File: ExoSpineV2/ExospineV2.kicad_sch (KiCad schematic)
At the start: 44 parts, among them J1 GPIO, J15 JST PH 2pin, J16 JST PH 2pin, J19 JST PH 3pin, J20 JST PH 3pin, J22 JST PH 2pin, J23 JST PH 2pin, J24 JST PH 2pin, J25 JST PH 3pin, J26 JST PH 3pin, J27 JST PH 4pin, J29 JST PH 3pin, J30 JST PH 2pin, J34 JST PH 3pin, Q10 Q_NMOS_DGS, Q11 Q_NMOS_DGS, Q6 Q_NMOS_DGS, Q7 Q_NMOS_DGS, Q9 Q_NMOS_DGS, U4 74HC00, U5 74HC00, U6 MCP3008, U7 LTC2944, U8 LTC2944

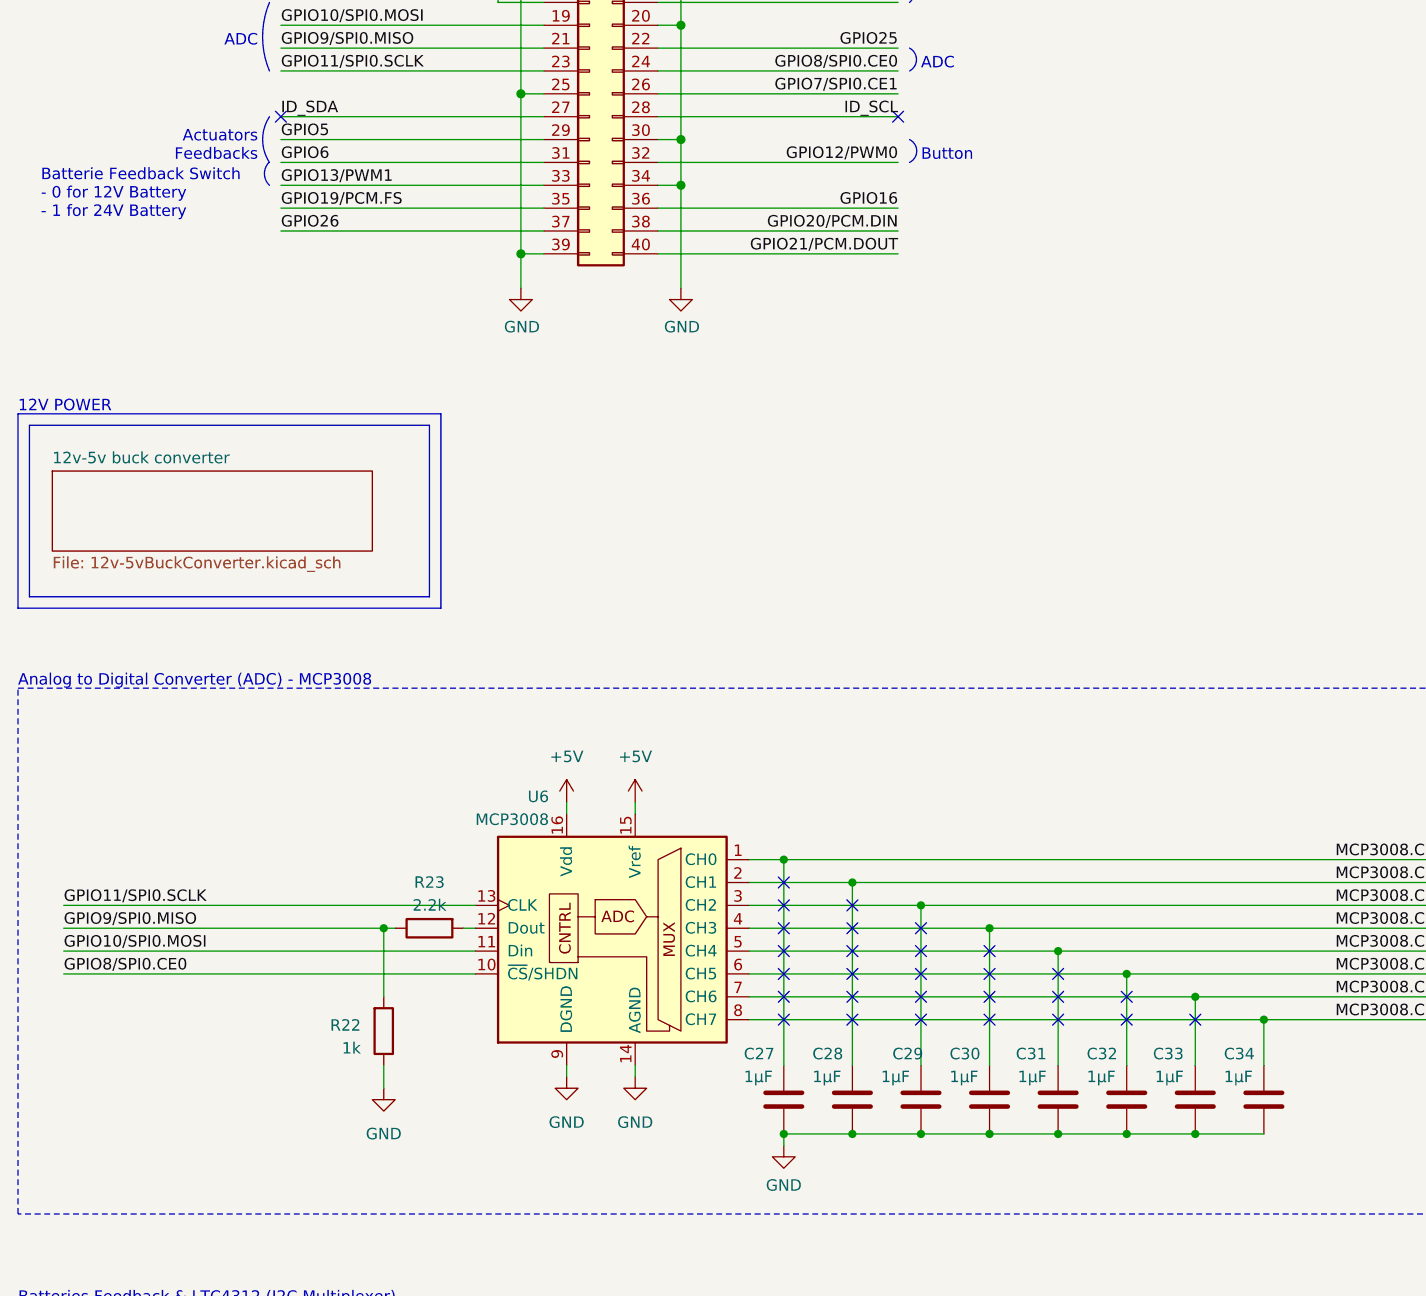
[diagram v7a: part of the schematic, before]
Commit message: chose resistors and capacitors
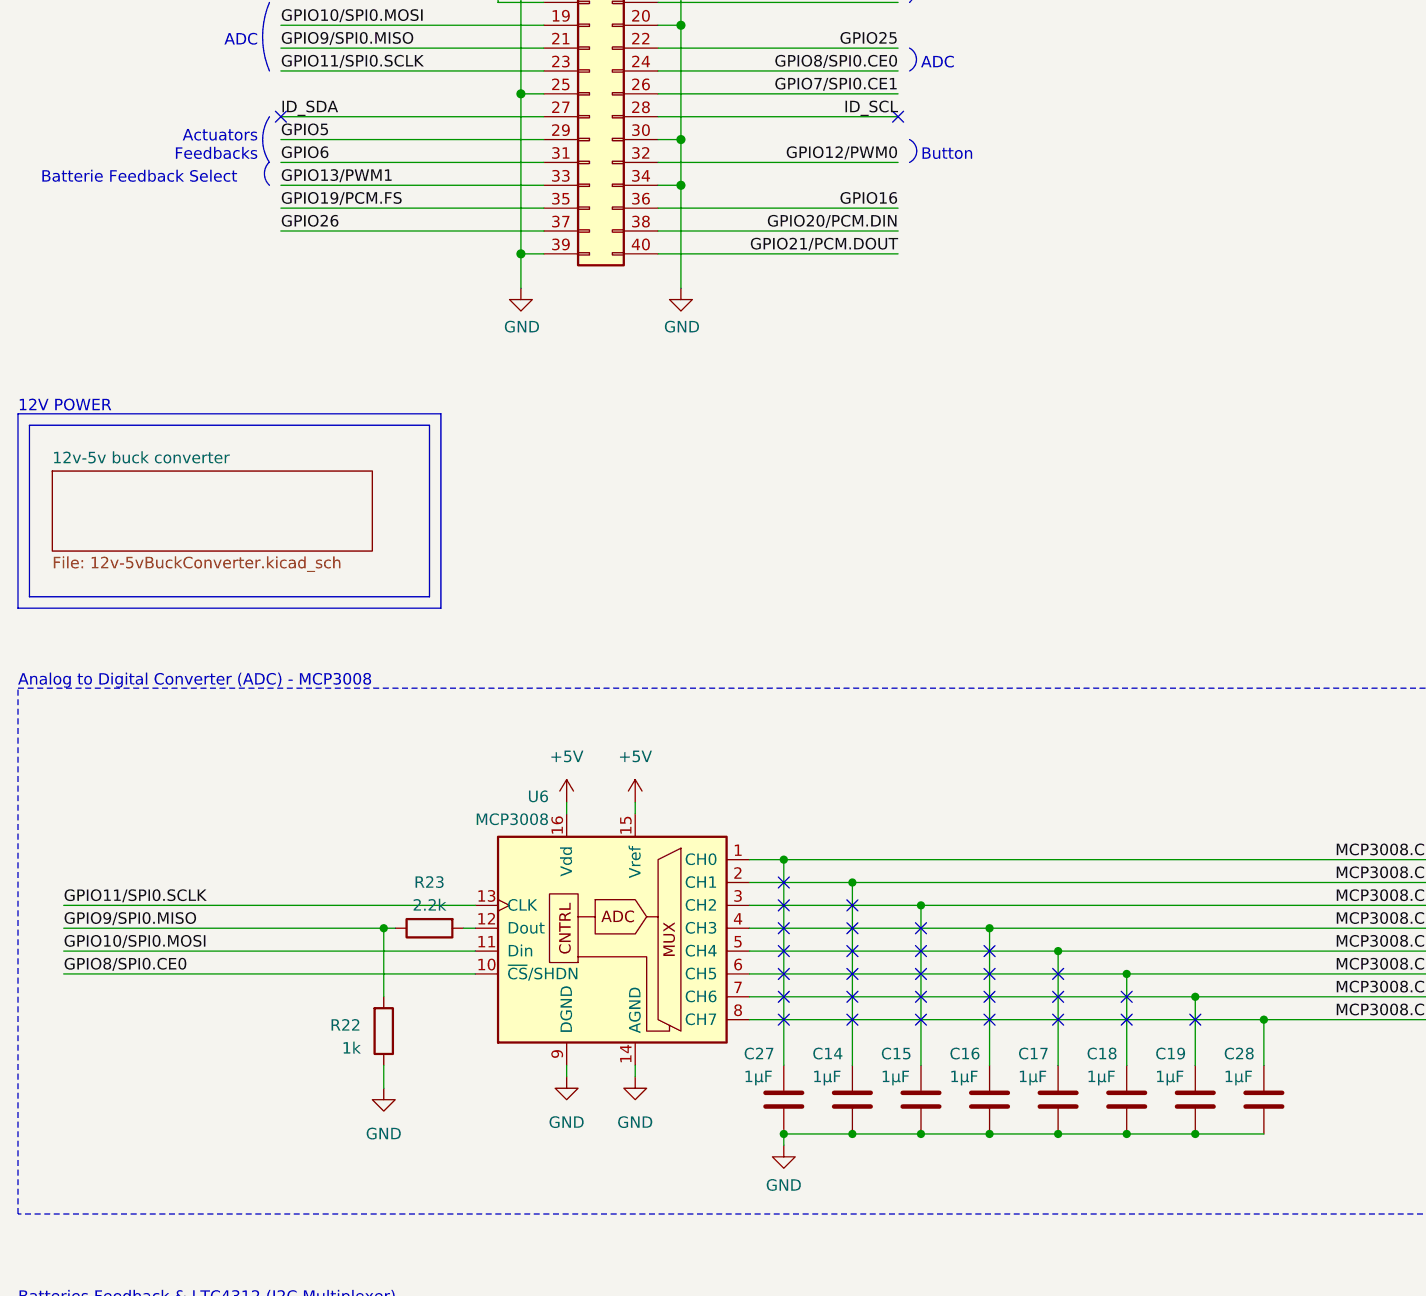
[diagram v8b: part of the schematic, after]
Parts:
- removed C29, C30, C31, C32, C33, C34: 1µF, symbol Device:C
- added C14, C15, C16, C17, C18, C19: 1µF, Capacitor_SMD:C_0603_1608Metric, symbol Device:C
- C27, C28: footprint (none) -> Capacitor_SMD:C_0603_1608Metric; JLCPCB (none) -> https://jlcpcb.com/partdetail/16531-CL10A105KB8NNNC/C15849
- R22: footprint (none) -> Resistor_SMD:R_0805_2012Metric; JLCPCB (none) -> https://jlcpcb.com/partdetail/18201-0805W8F1001T5E/C17513
- R23: footprint (none) -> Resistor_SMD:R_0805_2012Metric; JLCPCB (none) -> https://jlcpcb.com/partdetail/18208-0805W8F2201T5E/C17520
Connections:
- net GND: now also C14.2, C15.2, C16.2, C17.2, C18.2, C19.2
- net MCP3008.CH1: now also C14.1; no longer C28.1
- net MCP3008.CH2: now also C15.1
- net MCP3008.CH3: now also C16.1
- net MCP3008.CH4: now also C17.1
- net MCP3008.CH5: now also C18.1
- net MCP3008.CH6: now also C19.1
- net MCP3008.CH7: now also C28.1
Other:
- note added: "Batterie Feedback Select"
- note removed: "Batterie Feedback Switch - 0 for 12V Battery - 1 for 24V Battery"
